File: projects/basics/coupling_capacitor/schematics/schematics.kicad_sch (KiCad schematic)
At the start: 3 parts

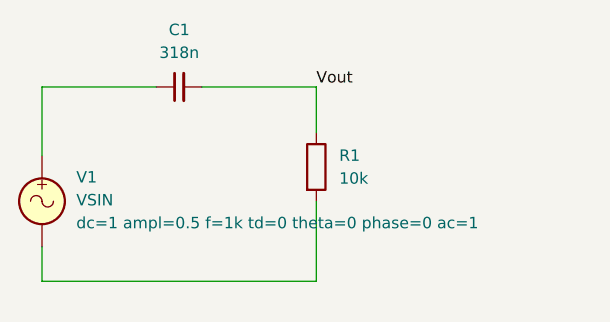
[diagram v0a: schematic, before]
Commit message: feat: updates to coupling capacitor projects
Adds scripts for generating the frequency response chart for the
coupling capacitor project based on gnuplot.

Updates descriptions of both simulations and measurements.

Fixes the missing schematics for the coupling capacitor project.

Breaking changes: None

Resolves: None
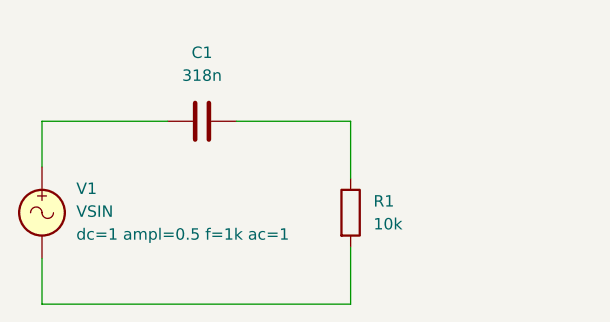
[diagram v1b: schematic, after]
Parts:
- removed C1: 318n, symbol Device:C_Small
- added C1: 318n, symbol Device:C
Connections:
- net at V1.1: now also C1.1
- net Vout: no longer names the net of R1.1
- net Vout: now also C1.2
